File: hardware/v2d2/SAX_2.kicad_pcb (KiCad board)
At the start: 2 copper layers, 80 parts, among them J1 Prog port, J2 SSD1306, U1 74HC165, U2 74HC165, U3 74HC165, U4 BluePill_STM32F103C

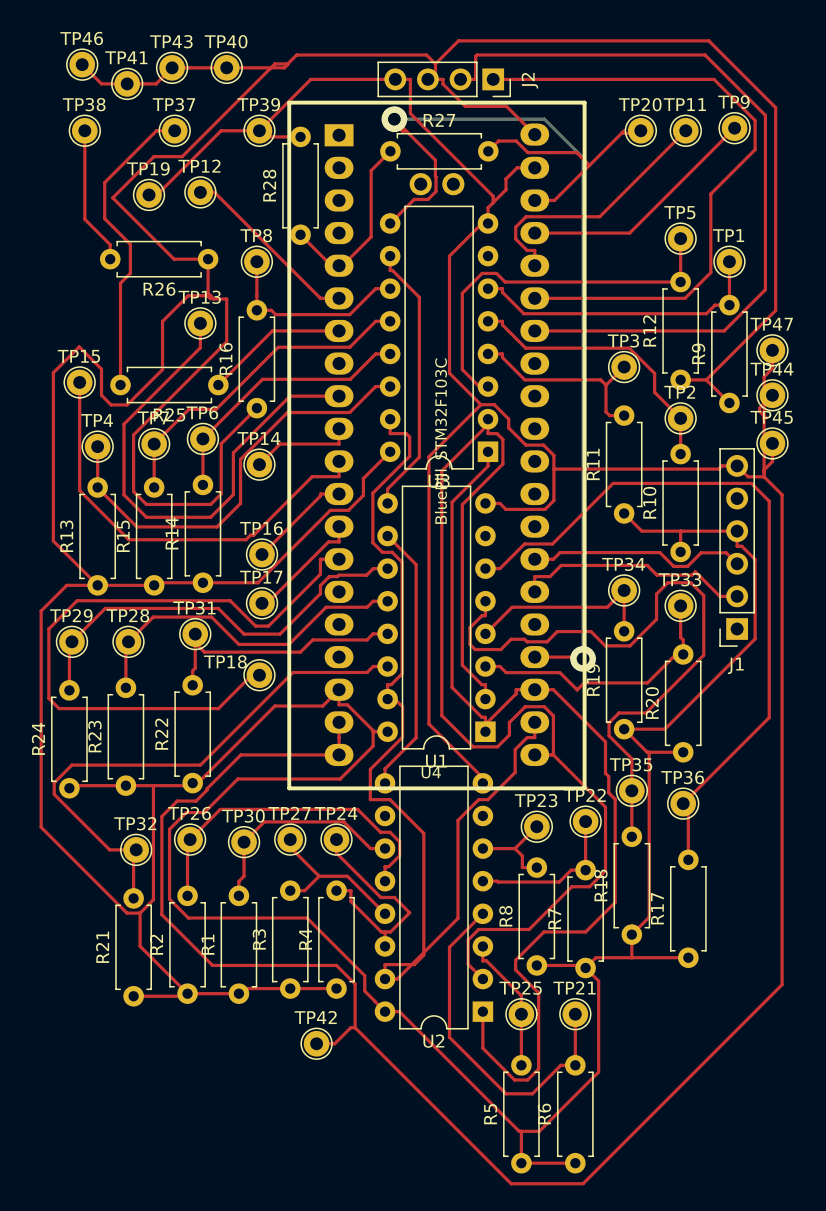
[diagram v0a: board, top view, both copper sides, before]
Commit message: Improved fab layer
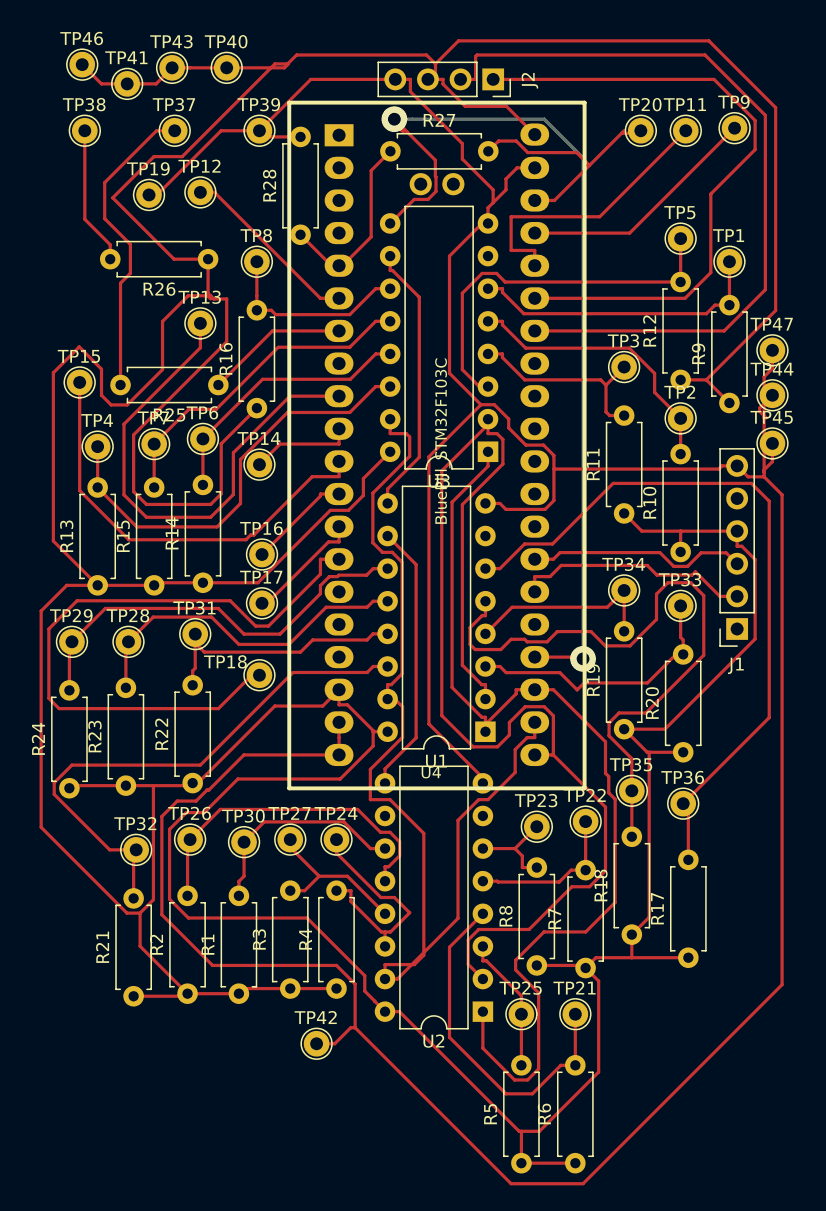
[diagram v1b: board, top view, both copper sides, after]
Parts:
- J2: value SSD1306 -> (GND) SSD1306
- R1, R10, R11, R12, R13, R14, R15, R16, R17, R18, R19, R2, R20, R21, R22, R23, R24, R3, R4, R5, R6, R7, R8, R9: value R -> 10k
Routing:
- net Net-(TP11-Pad1): track 20.3 -> 22.0 mm
